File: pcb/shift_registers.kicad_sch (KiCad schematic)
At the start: 8 parts, among them U1 IC_HV5622PG-G, U2 IC_HV5622PG-G

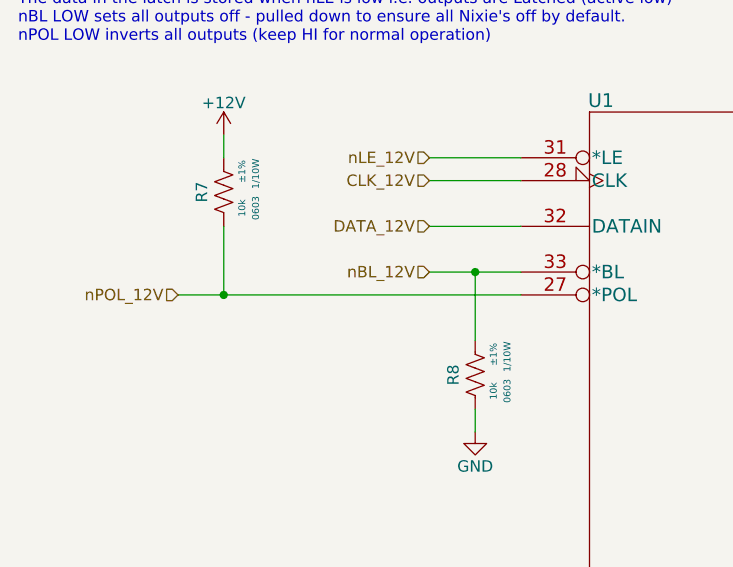
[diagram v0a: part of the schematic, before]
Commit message: Added LSE crystal and started configuring MCU Pinout"
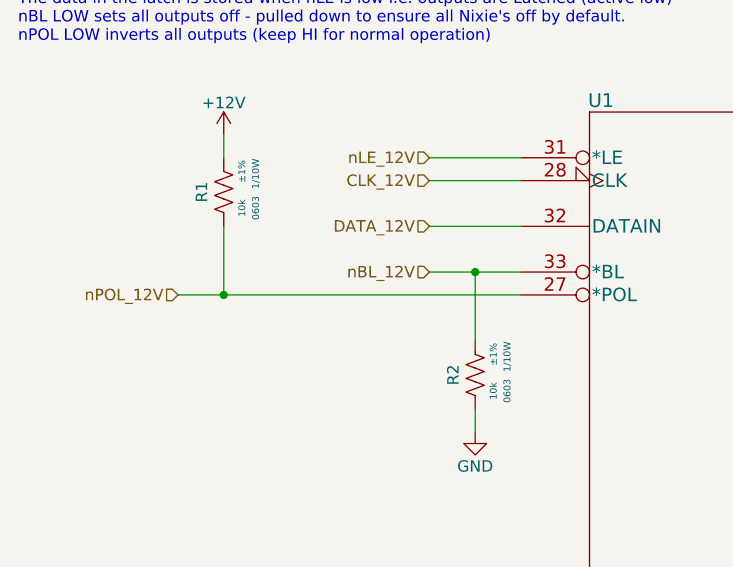
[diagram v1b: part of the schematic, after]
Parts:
- renumbered R7 to R1, R8 to R2
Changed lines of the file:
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@@
   (symbol (lib_id "power:+12V") (at 50.8 236.22 0) (unit 1)
     (in_bom yes) (on_board yes)
-    (property "Reference" "#PWR03" (id 0) (at 50.8 240.03 0)
+    (property "Reference" "#PWR05" (id 0) (at 50.8 240.03 0)
       (effects (font (size 1.27 1.27)) hide)
     )
@@
   (symbol (lib_id "arjun_symbols:RES_10K_1P_1{slash}10W_0603") (at 66.04 58.42 0) (unit 1)
     (in_bom yes) (on_board yes)
-    (property "Reference" "R8" (id 0) (at 62.865 62.23 90)
+    (property "Reference" "R2" (id 0) (at 62.865 62.23 90)
       (effects (font (size 1.27 1.27)) (justify top))
     )
@@
   (symbol (lib_id "power:GND") (at 66.04 68.58 0) (unit 1)
     (in_bom yes) (on_board yes)
-    (property "Reference" "#PWR013" (id 0) (at 66.04 74.93 0)
+    (property "Reference" "#PWR02" (id 0) (at 66.04 74.93 0)
       (effects (font (size 1.27 1.27)) hide)
     )
@@
   (symbol (lib_id "power:GND") (at 50.8 256.54 0) (unit 1)
     (in_bom yes) (on_board yes)
-    (property "Reference" "#PWR04" (id 0) (at 50.8 262.89 0)
+    (property "Reference" "#PWR06" (id 0) (at 50.8 262.89 0)
       (effects (font (size 1.27 1.27)) hide)
     )
@@
   (symbol (lib_id "power:+12V") (at 38.1 35.56 0) (unit 1)
     (in_bom yes) (on_board yes)
-    (property "Reference" "#PWR012" (id 0) (at 38.1 39.37 0)
+    (property "Reference" "#PWR01" (id 0) (at 38.1 39.37 0)
       (effects (font (size 1.27 1.27)) hide)
     )
@@
   (symbol (lib_id "arjun_symbols:RES_10K_1P_1{slash}10W_0603") (at 38.1 38.1 0) (unit 1)
     (in_bom yes) (on_board yes)
-    (property "Reference" "R7" (id 0) (at 34.925 41.91 90)
+    (property "Reference" "R1" (id 0) (at 34.925 41.91 90)
       (effects (font (size 1.27 1.27)) (justify top))
     )
@@
   (symbol (lib_id "power:+12V") (at 50.8 111.76 0) (unit 1)
     (in_bom yes) (on_board yes)
-    (property "Reference" "#PWR01" (id 0) (at 50.8 115.57 0)
+    (property "Reference" "#PWR03" (id 0) (at 50.8 115.57 0)
       (effects (font (size 1.27 1.27)) hide)
     )
@@
   (symbol (lib_id "power:GND") (at 50.8 132.08 0) (unit 1)
     (in_bom yes) (on_board yes)
-    (property "Reference" "#PWR02" (id 0) (at 50.8 138.43 0)
-      (effects (font (size 1.27 1.27)) hide)
-    )
+    (property "Reference" "#PWR04" (id 0) (at 50.8 138.43 0)
+      (effects (font (size 1.27 1.27)) hide)
+    )

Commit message: Added 8MHz Oscillator and mapped most of the MCU pins"
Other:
- note added: "!!ADD DOTS"
- note added: "CLK transitions on falling edge Transfer of data from the Shift register to the latch occurs when the nLE input is high. (When active low the data is latched and not shown to the output.) The data in the latch is stored when nLE is low i.e. outputs are Latched (active low) nBL LOW sets all outputs off - pulled down to ensure all Nixie's off by default. nPOL LOW inverts all outputs (keep HI for no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"
- note removed: "CLK transitions on falling edge Transfer of data from the Shift register to the latch occurs when the nLE input is high. The data in the latch is stored when nLE is low i.e. outputs are Latched (active low) nBL LOW sets all outputs off - pulled down to ensure all Nixie's off by default. nPOL LOW inverts all outputs (keep HI for normal operation)"
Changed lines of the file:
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@@
     (stroke (width 0) (type default) (color 0 0 0 0))
   )
-  (text "CLK transitions on falling edge\nTransfer of data from the Shift register to the latch occurs when the nLE input is high. \nThe data in the latch is stored when nLE is low i.e. outputs are Latched (active low)\nnBL LOW sets all outputs off - pulled down to ensure all Nixie's off by default.\nnPOL LOW inverts all outputs (keep HI for normal operation)\n"
+  (text "CLK transitions on falling edge\nTransfer of data from the Shift register to the latch occurs when the nLE input is high. (When active low the data is latched and not shown to the output.)\nThe data in the latch is stored when nLE is low i.e. outputs are Latched (active low)\nnBL LOW sets all outputs off - pulled down to ensure all Nixie's off by default.\nnPOL LOW inverts all outputs (keep HI for normal operation)\n"
     (at 15.24 25.4 0)
     (effects (font (size 1.27 1.27)) (justify left bottom))
   )
+  (text "!!ADD DOTS\n" (at 320.04 111.76 0)
+    (effects (font (size 1.27 1.27)) (justify left bottom))
+  )

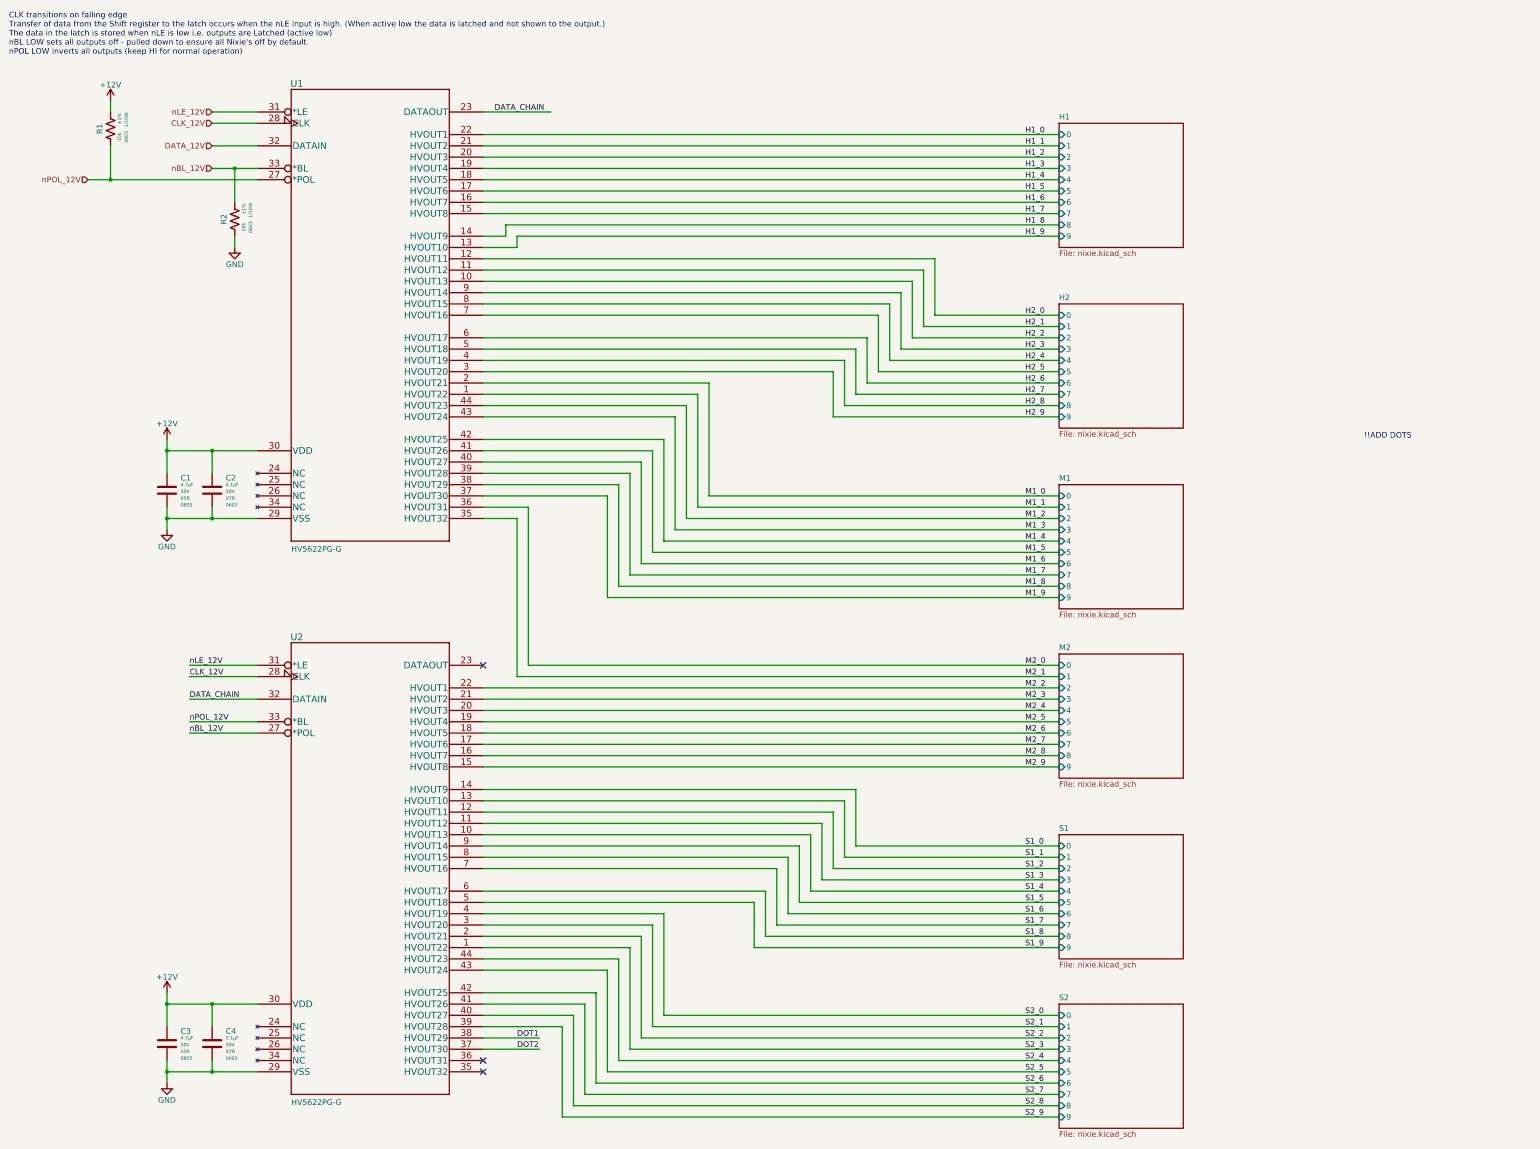
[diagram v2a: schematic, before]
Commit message: Added MCU pinouts for rotary encoder
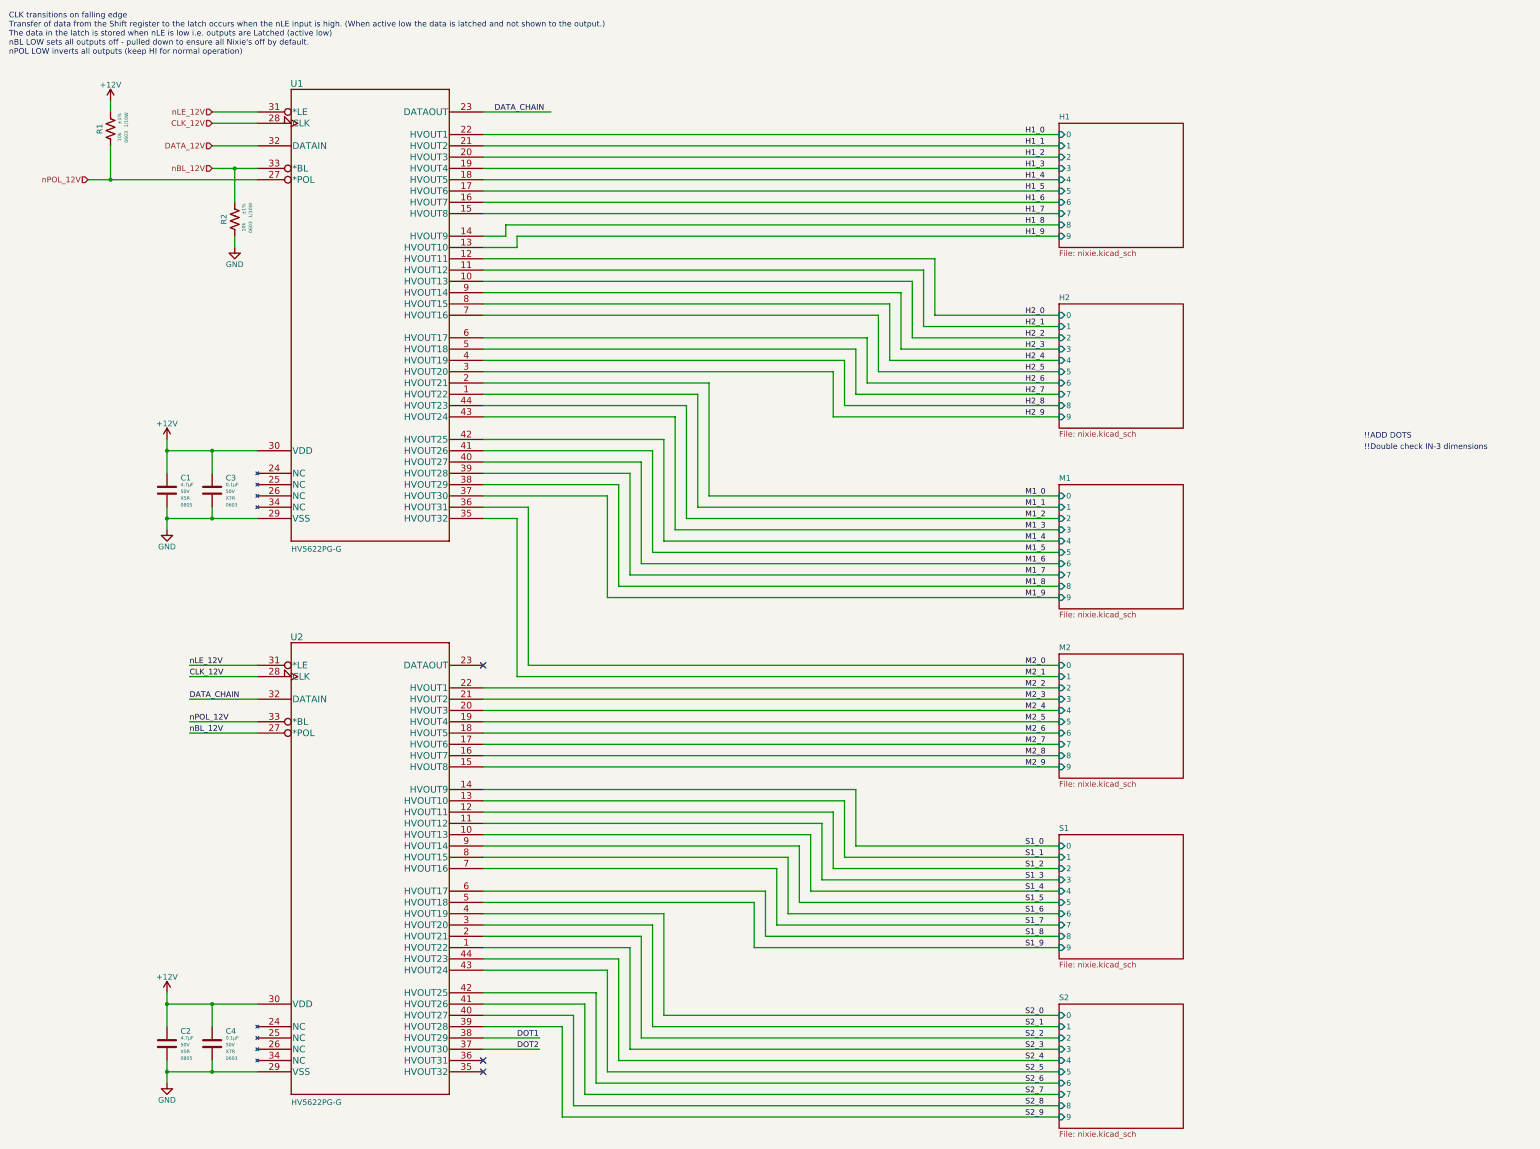
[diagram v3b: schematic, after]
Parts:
- renumbered C3 to C2, C2 to C3
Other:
- note added: "!!Double check IN-3 dimensions"
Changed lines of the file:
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@@
+    (effects (font (size 1.27 1.27)) (justify left bottom))
+  )
+  (text "!!Double check IN-3 dimensions\n" (at 320.04 114.3 0)
     (effects (font (size 1.27 1.27)) (justify left bottom))
   )
@@
   (symbol (lib_id "power:+12V") (at 50.8 236.22 0) (unit 1)
     (in_bom yes) (on_board yes)
-    (property "Reference" "#PWR05" (id 0) (at 50.8 240.03 0)
+    (property "Reference" "#PWR04" (id 0) (at 50.8 240.03 0)
       (effects (font (size 1.27 1.27)) hide)
     )
@@
   (symbol (lib_id "power:GND") (at 66.04 68.58 0) (unit 1)
     (in_bom yes) (on_board yes)
-    (property "Reference" "#PWR02" (id 0) (at 66.04 74.93 0)
+    (property "Reference" "#PWR06" (id 0) (at 66.04 74.93 0)
       (effects (font (size 1.27 1.27)) hide)
     )
@@
   (symbol (lib_id "power:GND") (at 50.8 256.54 0) (unit 1)
     (in_bom yes) (on_board yes)
-    (property "Reference" "#PWR06" (id 0) (at 50.8 262.89 0)
+    (property "Reference" "#PWR05" (id 0) (at 50.8 262.89 0)
       (effects (font (size 1.27 1.27)) hide)
     )
@@
   (symbol (lib_id "power:+12V") (at 50.8 111.76 0) (unit 1)
     (in_bom yes) (on_board yes)
-    (property "Reference" "#PWR03" (id 0) (at 50.8 115.57 0)
+    (property "Reference" "#PWR02" (id 0) (at 50.8 115.57 0)
       (effects (font (size 1.27 1.27)) hide)
     )
@@
   (symbol (lib_id "arjun_symbols:CAP_CER_0u1_50V_X7R_0603") (at 60.96 119.38 0) (unit 1)
     (in_bom yes) (on_board yes)
-    (property "Reference" "C2" (id 0) (at 64.008 120.396 0)
+    (property "Reference" "C3" (id 0) (at 64.008 120.396 0)
       (effects (font (size 1.27 1.27)) (justify left))
     )
@@
   (symbol (lib_id "power:GND") (at 50.8 132.08 0) (unit 1)
     (in_bom yes) (on_board yes)
-    (property "Reference" "#PWR04" (id 0) (at 50.8 138.43 0)
+    (property "Reference" "#PWR03" (id 0) (at 50.8 138.43 0)
       (effects (font (size 1.27 1.27)) hide)
     )
@@
   (symbol (lib_id "arjun_symbols:CAP_CER_4u7_50V_X5R_0805") (at 50.8 243.84 0) (unit 1)
     (in_bom yes) (on_board yes)
-    (property "Reference" "C3" (id 0) (at 53.848 244.856 0)
+    (property "Reference" "C2" (id 0) (at 53.848 244.856 0)
       (effects (font (size 1.27 1.27)) (justify left))
     )
